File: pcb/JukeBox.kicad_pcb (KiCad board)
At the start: 2 copper layers, 102 x 100 mm, 102 parts, among them J1 USB_C_Receptacle_USB2.0_16P, Q1 Q_NPN_BEC, SW1 SW_SPST, SW10 SW_SPST, SW11 SW_SPST, SW12 SW_SPST, SW2 SW_SPST, SW3 SW_SPST, SW4 SW_SPST, SW5 SW_SPST, SW6 SW_SPST, SW7 SW_SPST, SW8 SW_SPST, SW9 SW_SPST, U1 NCP1117-3.3_SOT223, U2 W25Q128JVS, U3 RP2350_60QFN, U5 CAT24C512, Y2 ABM8-272-T3

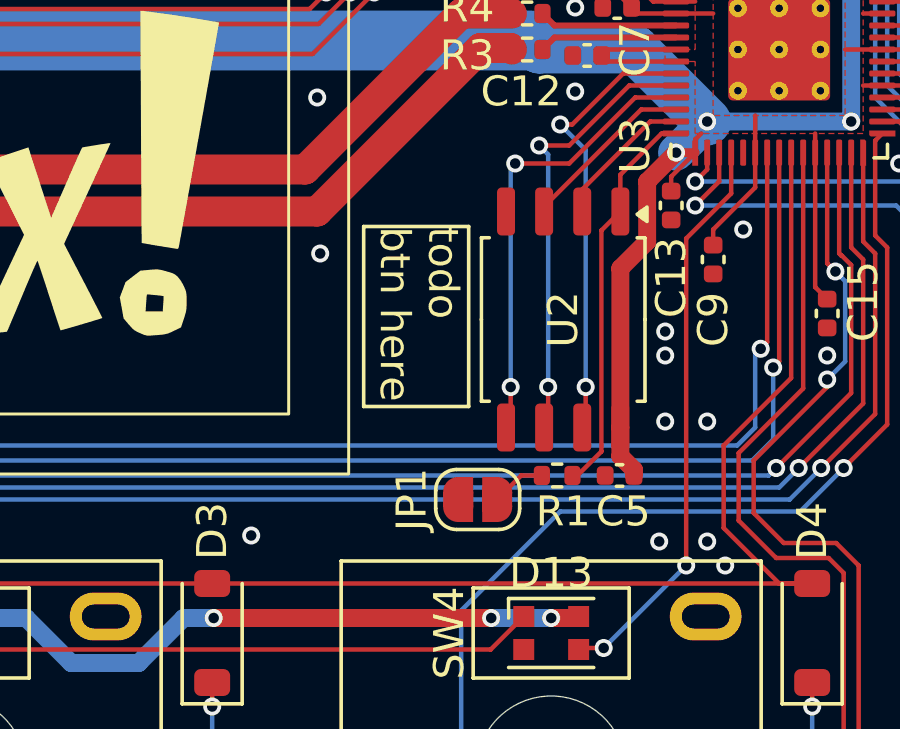
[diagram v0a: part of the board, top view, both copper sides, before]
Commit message: add bootsel button instead of pad
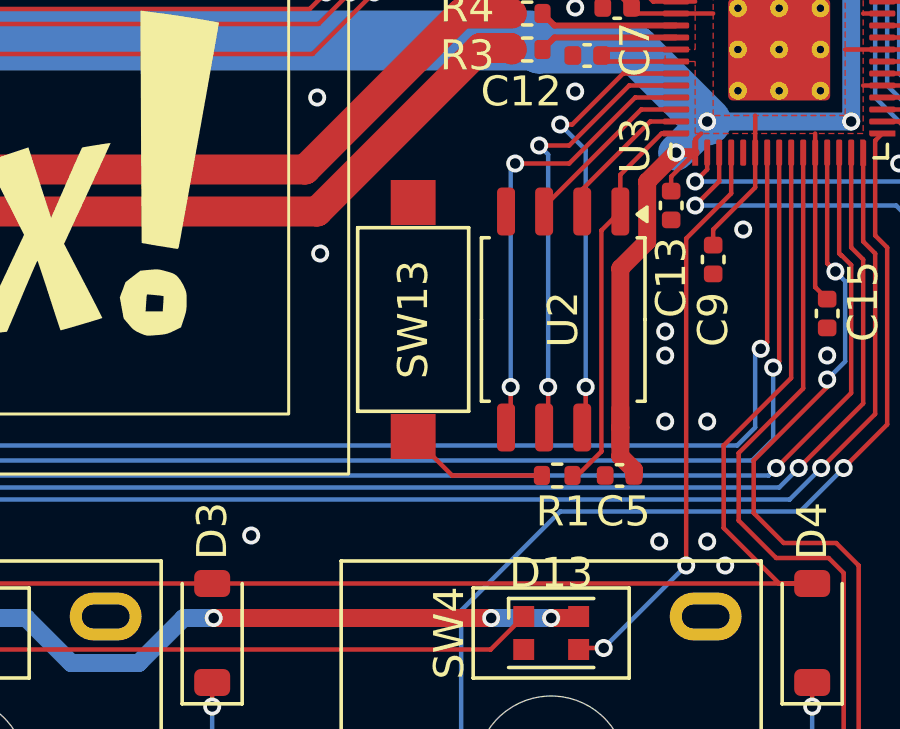
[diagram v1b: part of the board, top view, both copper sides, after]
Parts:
- removed JP1: SolderJumper_2_Open, Jumper:SolderJumper-2_P1.3mm_Open_RoundedPad1.0x1.5mm
- added SW13: SW_SPST, Button_Switch_SMD:SW_SPST_CK_RS282G05A3, F.Cu at (138.0, 96.8)
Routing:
- net /~{USB_BOOT}: track 1.82 -> 4.83 mm
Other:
- board text removed: "todo btn here"

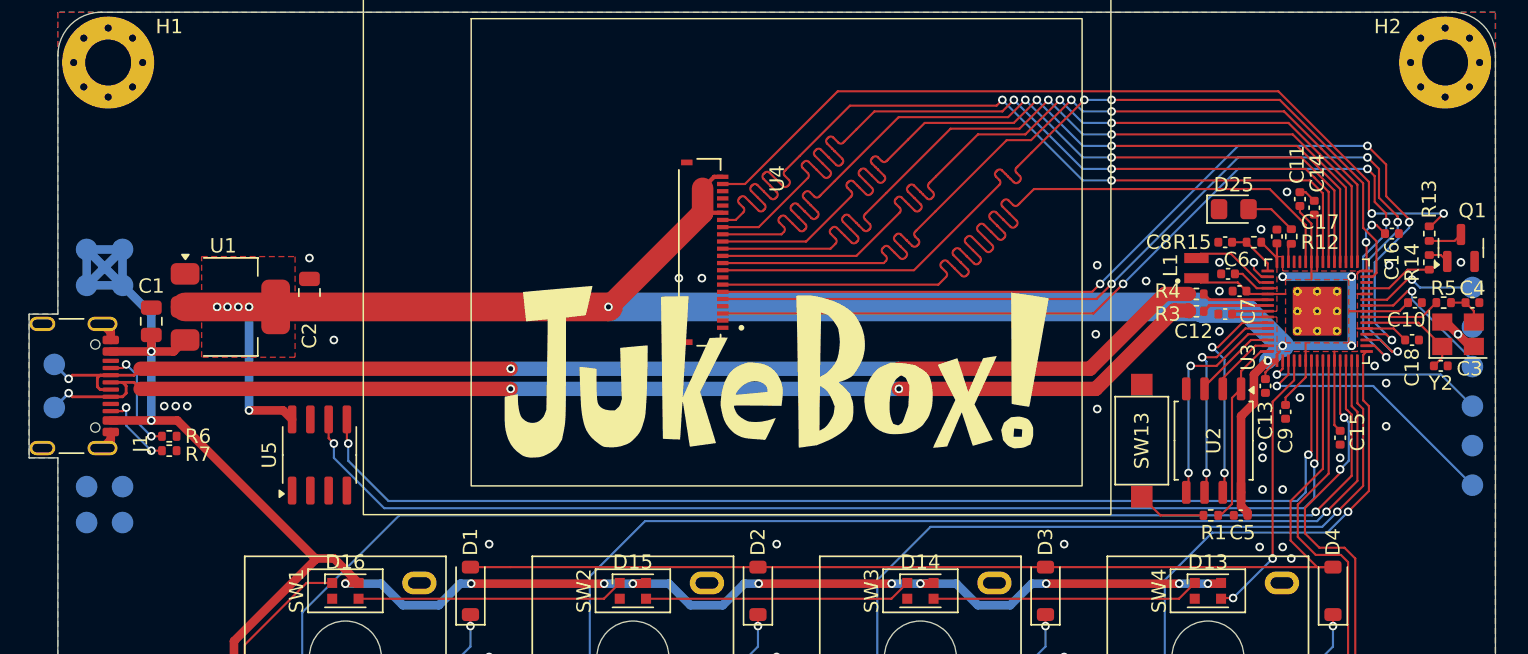
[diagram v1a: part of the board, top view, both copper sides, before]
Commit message: finalize pinout and routing for screen, add models for missing components
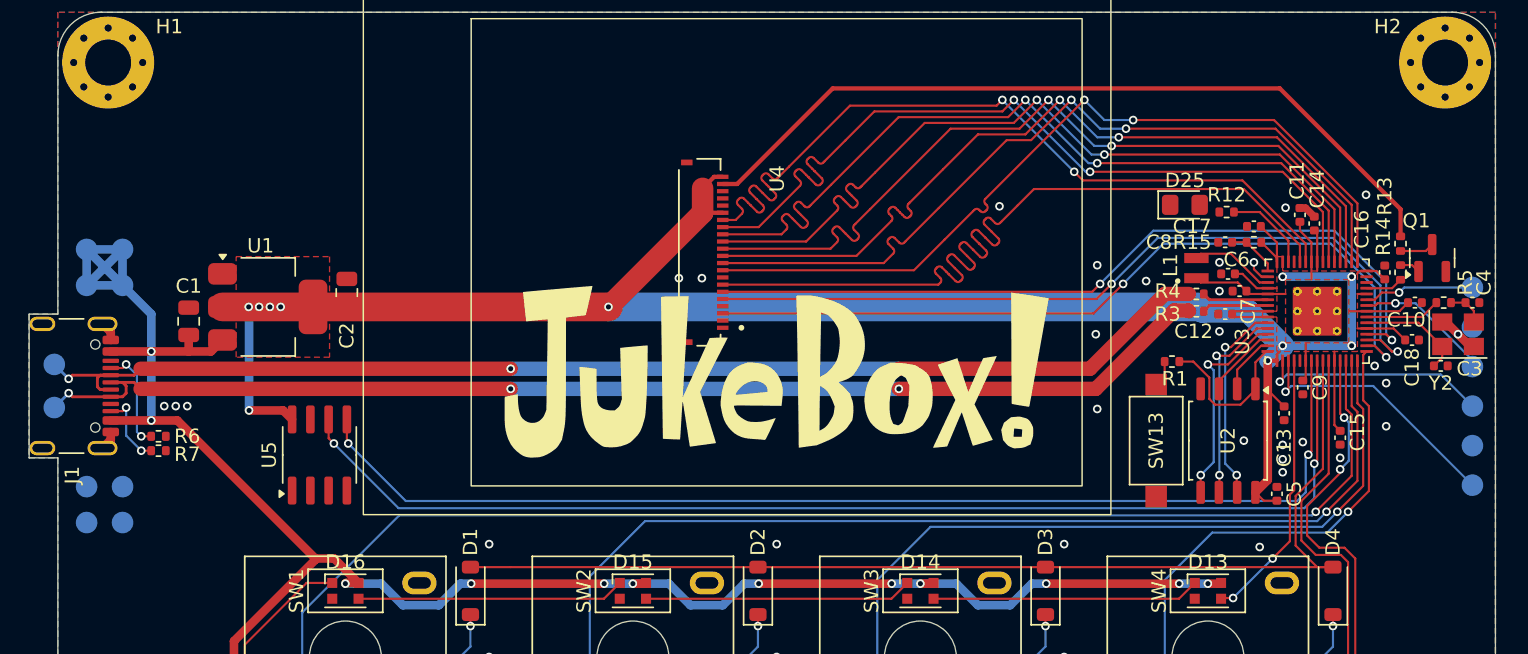
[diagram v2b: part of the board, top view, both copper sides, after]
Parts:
- moved R1 11.0 mm to (140.1, 91.3)
- moved R12 4.81 mm to (143.9, 80.9), turned to 180 degrees
- moved D25 3.41 mm to (141.0, 80.4)
- moved C5 2.93 mm to (147.4, 100.5), turned to 90 degrees
- moved C16 2.75 mm to (154.9, 85.1), turned to 90 degrees
- moved C1 2.60 mm to (71.7, 88.5)
- moved C2 2.60 mm to (82.7, 86.5)
- moved U1 2.60 mm to (77.2, 87.5)
- moved C13 2.30 mm to (147.9, 94.9)
- moved Q1 2.12 mm to (158.2, 84.1)
- moved R13 2.12 mm to (156.0, 83.1)
- moved R14 2.12 mm to (156.0, 85.1)
- moved C9 2.08 mm to (149.2, 93.1)
- moved C17 1.75 mm to (145.8, 81.9), turned to 180 degrees
- moved C14 1.10 mm to (150.0, 81.7)
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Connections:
- U3 pad 29: /SCRD0 -> /GPIO18
- U3 pad 31: /SCRD1 -> /SCRD0
- U3 pad 32: /SCRD2 -> /SCRD1
- U3 pad 33: /SCRD3 -> /SCRD2
- U3 pad 34: /SCRD4 -> /SCRD3
- U3 pad 35: /SCRD5 -> /SCRD4
- U3 pad 36: /SCRD6 -> /SCRD5
- U3 pad 37: /SCRD7 -> /SCRD6
- U3 pad 40: /SCRCLK -> /SCRD7
- U3 pad 41: /GPIO27_ADC1 -> /SCRCLK
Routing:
- net /SCRDC: track 67.2 -> 55.5 mm, vias 4 -> 2
- net /SCRCS: track 67.7 -> 56.7 mm, vias 4 -> 2
- net /SCRRST: track 65.7 -> 55.5 mm, vias 4 -> 2
- net /SCRD0: track 61.9 -> 56.9 mm
- net /SCRD7: track 61.8 -> 56.8 mm
- net /SCRCLK: track 64.8 -> 59.8 mm
- net /SCRD4: track 61.8 -> 56.8 mm
- net /SCRD6: track 61.8 -> 56.8 mm
- net /SCRD2: track 61.8 -> 56.9 mm
- net /SCRD3: track 61.8 -> 56.9 mm
- net /SCRD5: track 61.8 -> 56.8 mm
- net /SCRD1: track 61.8 -> 56.9 mm
- net /LEDPIN: track 1.34 -> 6.08 mm
- net /LEDK: track 58.9 -> 55.3 mm, vias 2 -> 0
- net Net-(D25-A): track 3.55 -> 0.00 mm
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
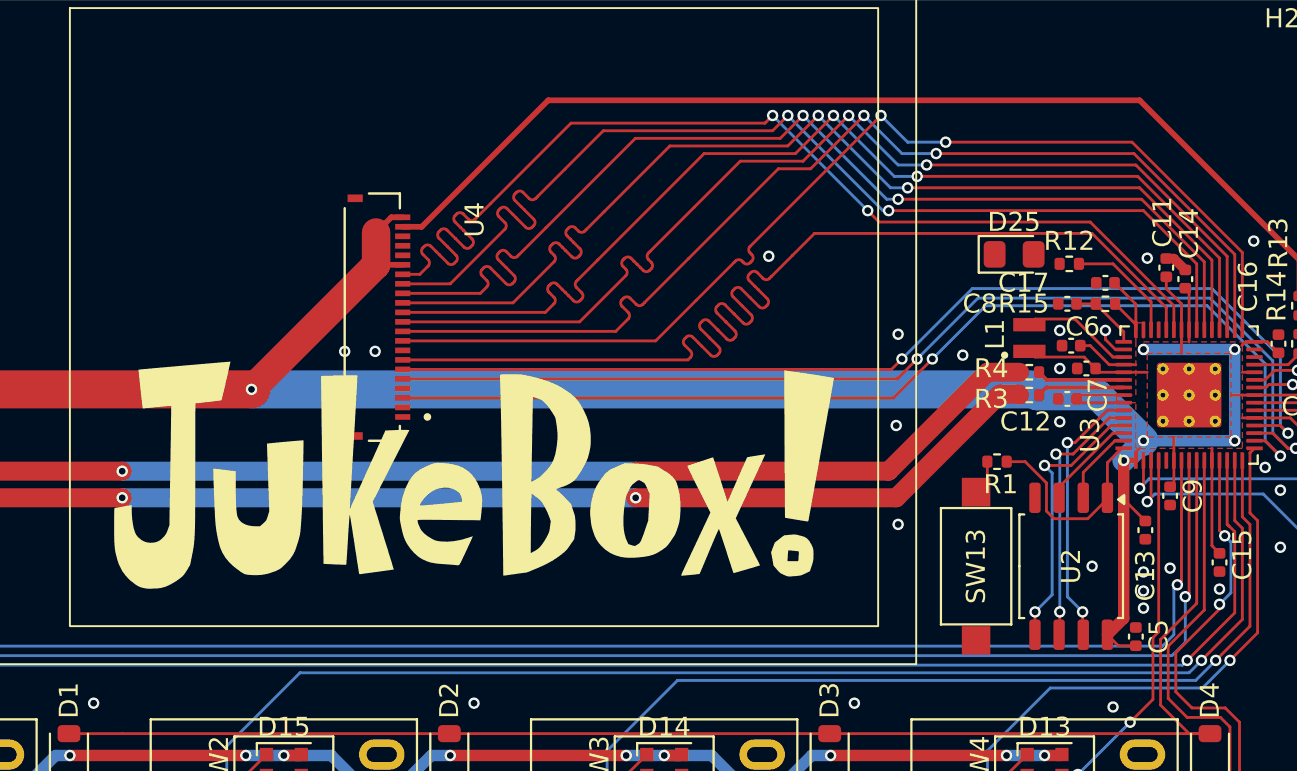
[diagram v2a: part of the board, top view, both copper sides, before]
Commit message: update footprint, do drc checking, ready for order
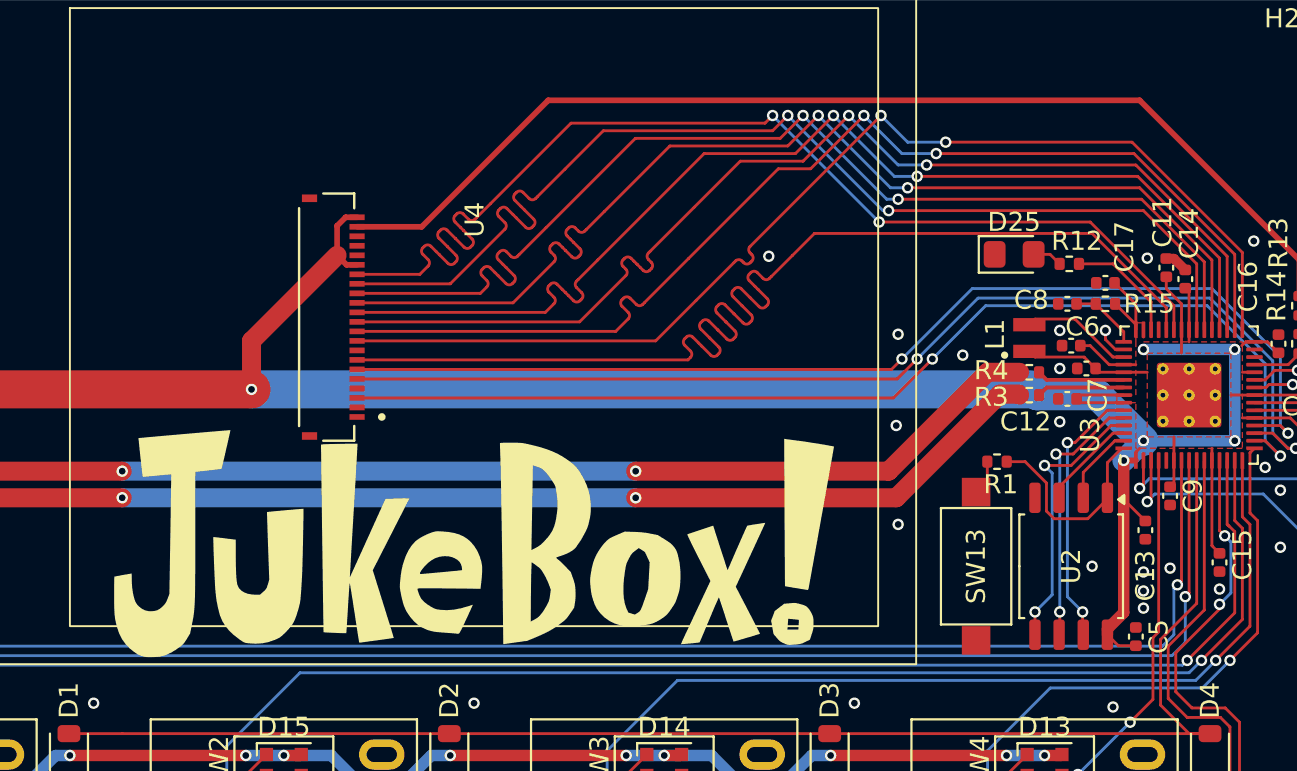
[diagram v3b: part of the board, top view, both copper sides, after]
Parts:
- moved G1 3.60 mm to (112.6, 95.6)
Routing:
- net /SCRD2: track 56.9 -> 59.3 mm
- net /SCRCLK: track 59.8 -> 62.2 mm
- net /SCRD4: track 56.8 -> 59.2 mm
- net /SCRRST: track 55.5 -> 57.9 mm
- net /SCRDC: track 55.5 -> 57.9 mm
- net /SCRD6: track 56.8 -> 59.2 mm
- net /SCRD5: track 56.8 -> 59.2 mm
- net /SCRD3: track 56.9 -> 59.3 mm
- net /SCRD1: track 56.9 -> 59.3 mm
- net /SCRD0: track 56.9 -> 59.3 mm
- net /LEDK: track 55.3 -> 57.7 mm
- net /SCRCS: track 56.7 -> 59.1 mm
- net /SCRD7: track 56.8 -> 59.2 mm
- net Net-(D25-A): track 0.00 -> 1.57 mm
- net +3V3: track 162.3 -> 161.2 mm
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
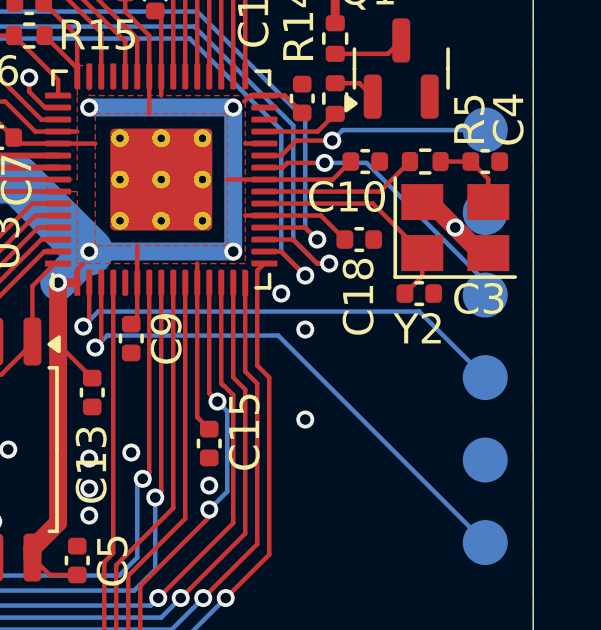
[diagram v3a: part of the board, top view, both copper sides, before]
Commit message: fix designator for clock crystal
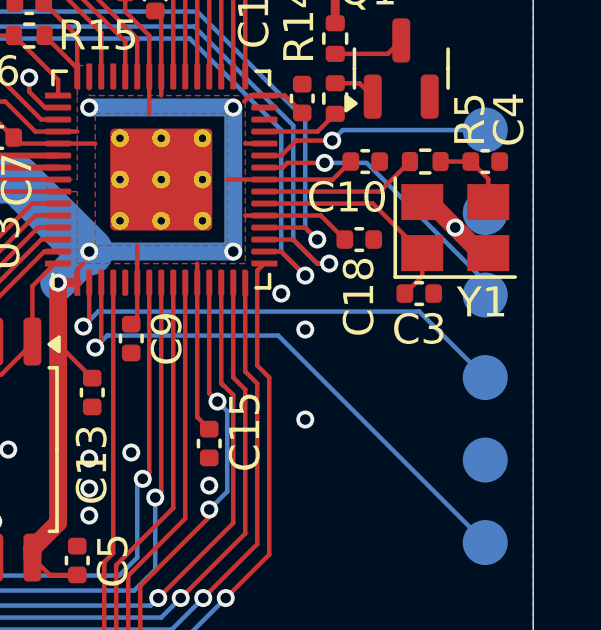
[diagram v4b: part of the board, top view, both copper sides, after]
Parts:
- renumbered Y2 to Y1
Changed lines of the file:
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@@
 		(tags "capacitor")
 		(property "Reference" "C3"
-			(at 2 0.2 0)
+			(at 0 1.2 0)
 			(layer "F.SilkS")
 			(effects
@@
 		(descr "Abracon Miniature Ceramic Smd Crystal ABM8G http://www.abracon.com/Resonators/ABM8G.pdf, 3.2x2.5mm^2 package")
 		(tags "SMD SMT crystal")
-		(property "Reference" "Y2"
-			(at -1.2 3.4 180)
+		(property "Reference" "Y1"
+			(at 0.9 2.5 180)
 			(layer "F.SilkS")
 			(effects

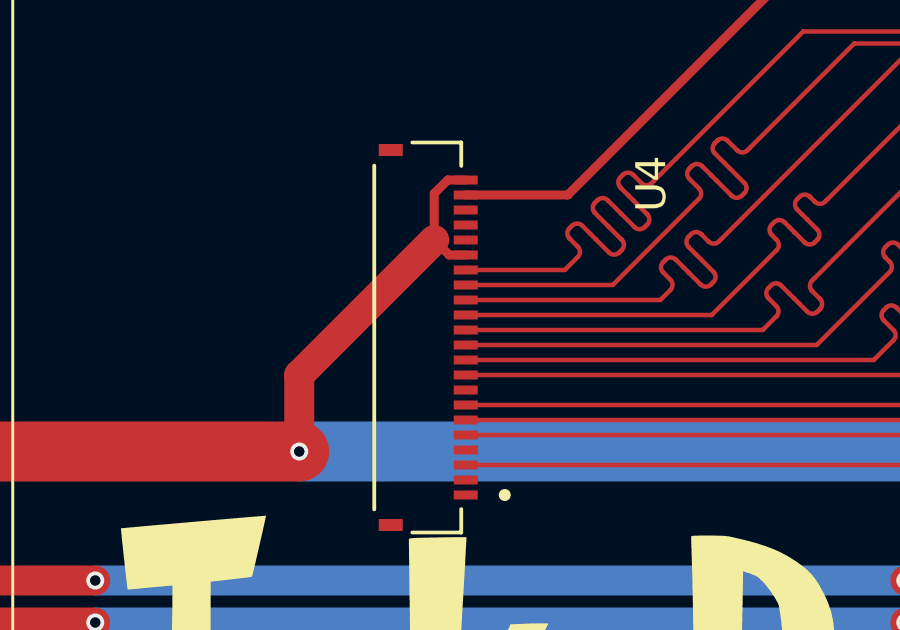
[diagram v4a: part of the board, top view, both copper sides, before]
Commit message: fix floating read clock on screen, which causes the screen to hang on startup
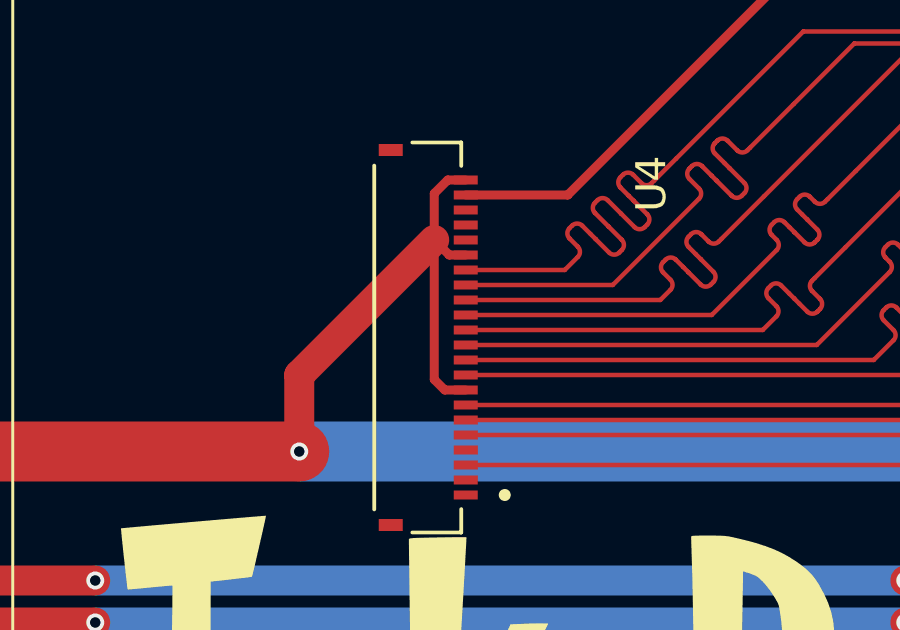
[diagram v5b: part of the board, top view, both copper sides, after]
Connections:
- U4 pad 15: unconnected-(U4-RD-Pad15) -> +3V3
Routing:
- net +3V3: track 161.2 -> 167.1 mm
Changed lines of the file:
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@@
 	(net 85 "unconnected-(U4-NC-Pad3)")
 	(net 86 "unconnected-(U4-NC-Pad4)")
-	(net 87 "unconnected-(U4-RD-Pad15)")
-	(net 88 "unconnected-(U4-TE-Pad19)")
-	(net 89 "unconnected-(U4-NC-Pad5)")
+	(net 87 "unconnected-(U4-TE-Pad19)")
+	(net 88 "unconnected-(U4-NC-Pad5)")
 	(footprint "LED_SMD:LED_WS2812B-2020_PLCC4_2.0x2.0mm"
 		(layer "F.Cu")
@@
 			(size 0.3 0.8)
 			(layers "F.Cu" "F.Mask")
-			(net 89 "unconnected-(U4-NC-Pad5)")
+			(net 88 "unconnected-(U4-NC-Pad5)")
 			(pinfunction "NC")
 			(pintype "no_connect")
@@
 			(size 0.3 0.8)
 			(layers "F.Cu" "F.Mask")
-			(net 87 "unconnected-(U4-RD-Pad15)")
+			(net 5 "+3V3")
 			(pinfunction "RD")
-			(pintype "input+no_connect")
+			(pintype "input")
 			(solder_mask_margin 0.102)
 		)
@@
 			(size 0.3 0.8)
 			(layers "F.Cu" "F.Mask")
-			(net 88 "unconnected-(U4-TE-Pad19)")
+			(net 87 "unconnected-(U4-TE-Pad19)")
 			(pinfunction "TE")
 			(pintype "input+no_connect")
@@
 	)
 	(segment
+		(start 105.74 85.45)
+		(end 106.44 85.45)
+		(width 0.3)
+		(layer "F.Cu")
+		(net 5)
+	)
+	(segment
 		(start 146.7525 99.2375)
 		(end 145.895 100.095)
@@
 	)
 	(segment
+		(start 105.39 80.45)
+		(end 105.39 85.1)
+		(width 0.3)
+		(layer "F.Cu")
+		(net 5)
+	)
+	(segment
 		(start 154.31 85)
 		(end 154.89 85.58)
@@
 		(layer "F.Cu")
 		(net 5)
+	)
+	(segment
+		(start 105.39 85.1)
+		(end 105.74 85.45)
+		(width 0.3)
+		(layer "F.Cu")
+		(net 5)
